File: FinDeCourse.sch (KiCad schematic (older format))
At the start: 2 parts, among them J14 butee

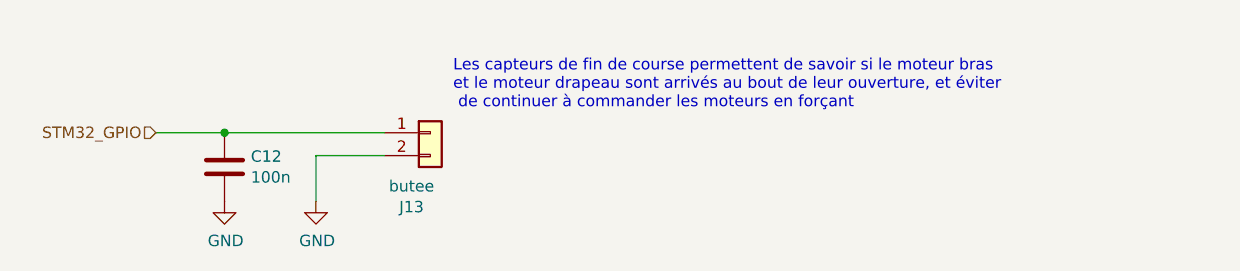
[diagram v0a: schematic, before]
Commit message: addition of second motor and ArUco outputs, note the last edition is the one called gange
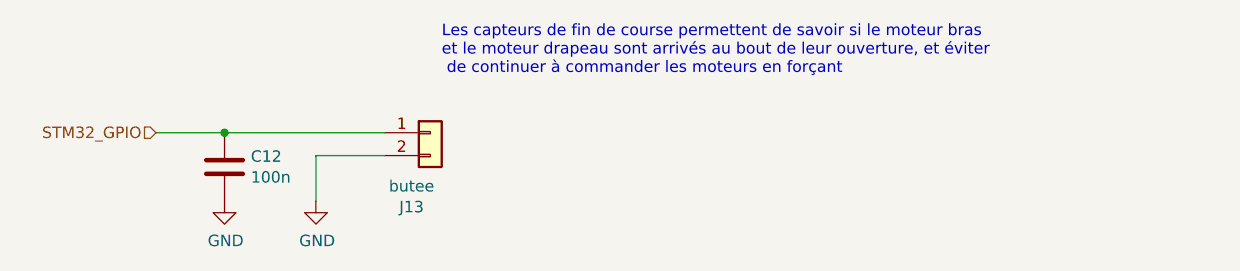
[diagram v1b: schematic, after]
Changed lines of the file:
@@
 $Descr A4 11693 8268
 encoding utf-8
-Sheet 22 24
+Sheet 23 24
 Title ""
 Date ""
@@
 	1    0    0    -1
 $EndComp
-Text Notes 7450 2500 0    50   ~ 0
+Text Notes 7400 2350 0    50   ~ 0
 Les capteurs de fin de course permettent de savoir si le moteur bras \net le moteur drapeau sont arrivés au bout de leur ouverture, et éviter\n de continuer à commander les moteurs en forçant
 $Comp

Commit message: removed psi-things pins, added transceiver MCP2551 for CAN, changed motors input protocol, RS must be chosen 1 or 10 kohms, and a foot print for a potentitial 120 ohms resistor is present for CAN bus end.
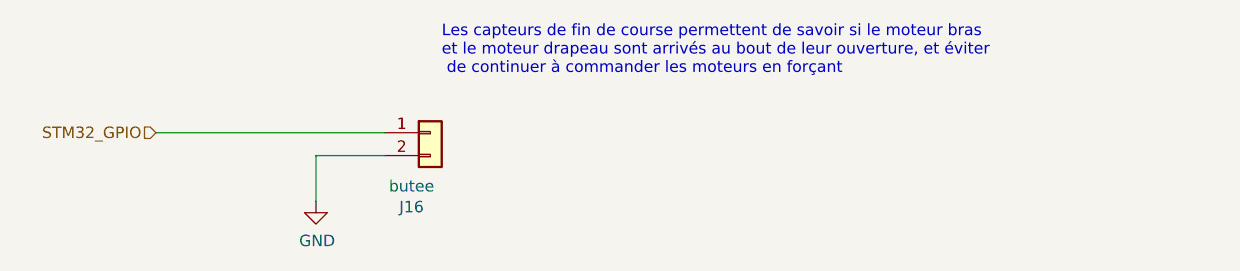
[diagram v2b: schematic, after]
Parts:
- removed C12: 100n, Capacitor_SMD:C_0805_2012Metric_Pad1.15x1.40mm_HandSolder, symbol shield_etage2-rescue:C-Device-shield_etage2-rescue
- renumbered J14 to J13
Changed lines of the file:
@@
 $Descr A4 11693 8268
 encoding utf-8
-Sheet 23 24
+Sheet 21 23
 Title ""
 Date ""
@@
 STM32_GPIO
 $Comp
-L shield_etage2-rescue:Conn_01x02-Connector_Generic-shield_etage2-rescue J14
+L shield_etage2-rescue:Conn_01x02-Connector_Generic-shield_etage2-rescue J13
 U 1 1 5E7DC2F9
 P 7350 2600
-AR Path="/5E6942FF/5E7DC2F9" Ref="J14"  Part="1"
-AR Path="/5E69459B/5E7DC2F9" Ref="J13"  Part="1"
-AR Path="/5F7E85D4/5E7DC2F9" Ref="J18"  Part="1"
-F 0 "J13" H 7268 2275 50  0000 C CNN
+AR Path="/5E6942FF/5E7DC2F9" Ref="J13"  Part="1"
+AR Path="/5E69459B/5E7DC2F9" Ref="J16"  Part="1"
+AR Path="/5F7E85D4/5E7DC2F9" Ref="J15"  Part="1"
+F 0 "J16" H 7268 2275 50  0000 C CNN
 F 1 "butee" H 7268 2366 50  0000 C CNN
 F 2 "Connector_JST:JST_PH_B2B-PH-K_1x02_P2.00mm_Vertical" H 7350 2600 50  0001 C CNN
@@
 	1    0    0    -1
 $EndComp
-$Comp
-L shield_etage2-rescue:GND-power-shield_etage2-rescue #PWR054
-U 1 1 5E7E6F28
-P 6450 2900
-AR Path="/5E6942FF/5E7E6F28" Ref="#PWR054"  Part="1"
-AR Path="/5E69459B/5E7E6F28" Ref="#PWR052"  Part="1"
-AR Path="/5F7E85D4/5E7E6F28" Ref="#PWR069"  Part="1"
-F 0 "#PWR052" H 6450 2650 50  0001 C CNN
-F 1 "GND" H 6455 2727 50  0000 C CNN
-F 2 "" H 6450 2900 50  0001 C CNN
-F 3 "" H 6450 2900 50  0001 C CNN
-	1    6450 2900
-	1    0    0    -1
-$EndComp
 Text Notes 7400 2350 0    50   ~ 0
 Les capteurs de fin de course permettent de savoir si le moteur bras \net le moteur drapeau sont arrivés au bout de leur ouverture, et éviter\n de continuer à commander les moteurs en forçant
 $Comp
-L shield_etage2-rescue:C-Device-shield_etage2-rescue C12
-U 1 1 5E835C66
-P 6450 2750
-AR Path="/5E69459B/5E835C66" Ref="C12"  Part="1"
-AR Path="/5E6942FF/5E835C66" Ref="C13"  Part="1"
-AR Path="/5F7E85D4/5E835C66" Ref="C17"  Part="1"
-F 0 "C12" H 6565 2796 50  0000 L CNN
-F 1 "100n" H 6565 2705 50  0000 L CNN
-F 2 "Capacitor_SMD:C_0805_2012Metric_Pad1.15x1.40mm_HandSolder" H 6488 2600 50  0001 C CNN
-F 3 "~" H 6450 2750 50  0001 C CNN
-	1    6450 2750
-	1    0    0    -1
-$EndComp
-Connection ~ 6450 2600
-Wire Wire Line
-	6450 2600 6150 2600
-Wire Wire Line
-	6450 2600 7150 2600
-$Comp
-L shield_etage2-rescue:GND-power-shield_etage2-rescue #PWR055
+L shield_etage2-rescue:GND-power-shield_etage2-rescue #PWR048
 U 1 1 5E8388AC
 P 6850 2900
-AR Path="/5E6942FF/5E8388AC" Ref="#PWR055"  Part="1"
-AR Path="/5E69459B/5E8388AC" Ref="#PWR053"  Part="1"
-AR Path="/5F7E85D4/5E8388AC" Ref="#PWR070"  Part="1"
-F 0 "#PWR053" H 6850 2650 50  0001 C CNN
+AR Path="/5E6942FF/5E8388AC" Ref="#PWR048"  Part="1"
+AR Path="/5E69459B/5E8388AC" Ref="#PWR059"  Part="1"
+AR Path="/5F7E85D4/5E8388AC" Ref="#PWR058"  Part="1"
+F 0 "#PWR059" H 6850 2650 50  0001 C CNN
 F 1 "GND" H 6855 2727 50  0000 C CNN
 F 2 "" H 6850 2900 50  0001 C CNN
@@
 Wire Wire Line
 	6850 2700 7150 2700
+Wire Wire Line
+	6150 2600 7150 2600
 $EndSCHEMATC

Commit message: correction mm -> inch, empreinte du bouton
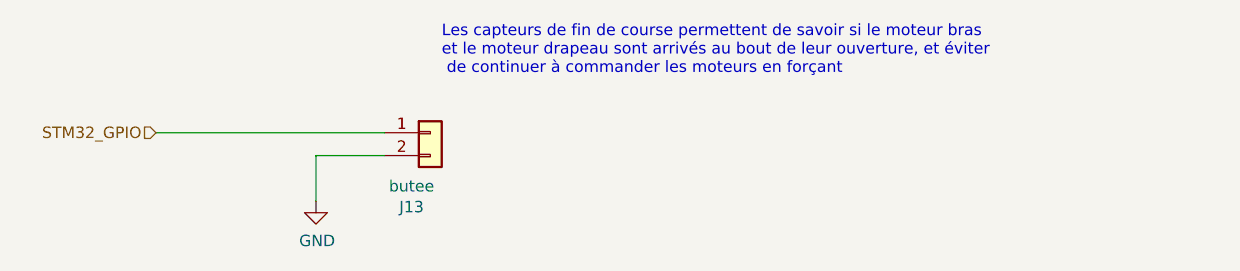
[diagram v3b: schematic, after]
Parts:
- J13: footprint Connector_JST:JST_PH_B2B-PH-K_1x02_P2.00mm_Vertical -> Connector_JST:JST_XH_B2B-XH-A_1x02_P2.50mm_Vertical
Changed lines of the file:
@@
 $Descr A4 11693 8268
 encoding utf-8
-Sheet 21 23
+Sheet 17 23
 Title ""
 Date ""
@@
 AR Path="/5E69459B/5E7DC2F9" Ref="J16"  Part="1"
 AR Path="/5F7E85D4/5E7DC2F9" Ref="J15"  Part="1"
-F 0 "J16" H 7268 2275 50  0000 C CNN
+F 0 "J13" H 7268 2275 50  0000 C CNN
 F 1 "butee" H 7268 2366 50  0000 C CNN
-F 2 "Connector_JST:JST_PH_B2B-PH-K_1x02_P2.00mm_Vertical" H 7350 2600 50  0001 C CNN
+F 2 "Connector_JST:JST_XH_B2B-XH-A_1x02_P2.50mm_Vertical" H 7350 2600 50  0001 C CNN
 F 3 "~" H 7350 2600 50  0001 C CNN
 	1    7350 2600
@@
 AR Path="/5E69459B/5E8388AC" Ref="#PWR059"  Part="1"
 AR Path="/5F7E85D4/5E8388AC" Ref="#PWR058"  Part="1"
-F 0 "#PWR059" H 6850 2650 50  0001 C CNN
+F 0 "#PWR048" H 6850 2650 50  0001 C CNN
 F 1 "GND" H 6855 2727 50  0000 C CNN
 F 2 "" H 6850 2900 50  0001 C CNN
